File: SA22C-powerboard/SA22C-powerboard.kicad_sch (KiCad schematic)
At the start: 22 parts, among them J1 Barrel_Jack_MountingPin, J4 Conn_01x09_Pin, J5 Conn_01x09_Pin, J6 Conn_01x02_Pin, J7 Conn_02x09_Odd_Even_MountingP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, U1 LM7805_TO220

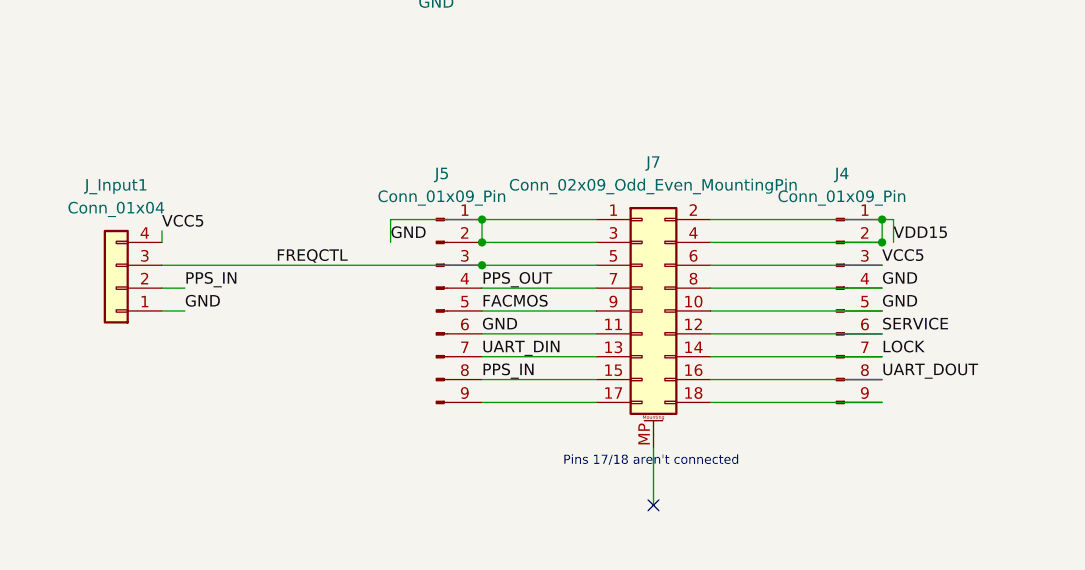
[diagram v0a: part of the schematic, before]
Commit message: Placement drafted, now on to gnd plane and cleanup/simplification
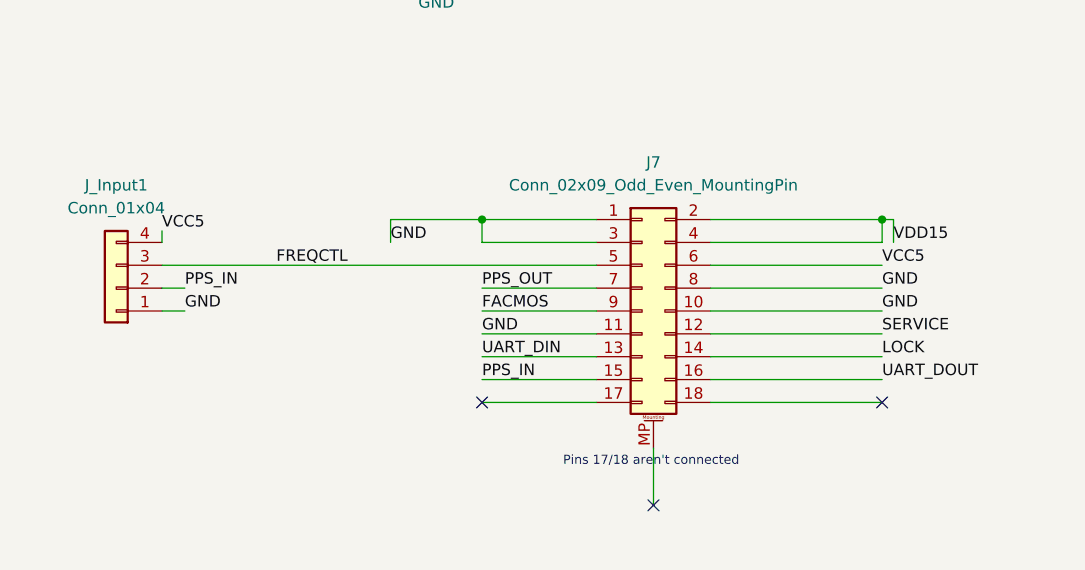
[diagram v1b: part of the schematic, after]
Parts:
- removed J4, J5: Conn_01x09_Pin, Connector_PinHeader_2.54mm:PinHeader_1x09_P2.54mm_Vertical, symbol Connector:Conn_01x09_Pin
- C3: footprint Capacitor_THT:C_Radial_D5.0mm_H11.0mm_P2.00mm -> Capacitor_SMD:CP_Elec_10x10
- C5: footprint Capacitor_SMD:CP_Elec_10x10 -> Capacitor_THT:C_Radial_D5.0mm_H11.0mm_P2.00mm
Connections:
- no-connect marks 1 -> 3
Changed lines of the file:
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@@
-	)
-	(junction
-		(at 118.11 85.09)
-		(diameter 0)
-		(color 0 0 0 0)
 	)
 	(junction
@@
 	)
 	(junction
-		(at 118.11 87.63)
-		(diameter 0)
-		(color 0 0 0 0)
-	)
-	(junction
 		(at 82.55 53.34)
 		(diameter 0)
@@
 	)
 	(junction
-		(at 162.56 85.09)
-		(diameter 0)
-		(color 0 0 0 0)
-	)
-	(junction
 		(at 76.2 34.29)
 		(diameter 0)
@@
 	)
 	(no_connect
+		(at 118.11 102.87)
+	)
+	(no_connect
 		(at 137.16 114.3)
 	)
+	(no_connect
+		(at 162.56 102.87)
+	)
 	(wire
 		(pts
@@
 	(wire
 		(pts
-			(xy 118.11 87.63) (xy 130.81 87.63)
+			(xy 82.55 87.63) (xy 130.81 87.63)
 		)
 		(stroke
@@
 		(pts
 			(xy 82.55 83.82) (xy 82.55 85.09)
-		)
-		(stroke
-			(width 0)
-			(type default)
-		)
-	)
-	(wire
-		(pts
-			(xy 82.55 87.63) (xy 118.11 87.63)
 		)
 		(stroke
@@
 	)
 	(symbol
-		(lib_id "Connector:Conn_01x09_Pin")
-		(at 113.03 92.71 0)
-		(unit 1)
-		(exclude_from_sim no)
-		(in_bom yes)
-		(on_board yes)
-		(dnp no)
-		(fields_autoplaced yes)
-		(property "Reference" "J5"
-			(at 113.665 77.47 0)
-			(effects
-				(font
-					(size 1.27 1.27)
-				)
-			)
-		)
-		(property "Value" "Conn_01x09_Pin"
-			(at 113.665 80.01 0)
-			(effects
-				(font
-					(size 1.27 1.27)
-				)
-			)
-		)
-		(property "Footprint" "Connector_PinHeader_2.54mm:PinHeader_1x09_P2.54mm_Vertical"
-			(at 113.03 92.71 0)
-			(effects
-				(font
-					(size 1.27 1.27)
-				)
-				(hide yes)
-			)
-		)
-		(property "Datasheet" "~"
-			(at 113.03 92.71 0)
-			(effects
-				(font
-					(size 1.27 1.27)
-				)
-				(hide yes)
-			)
-		)
-		(property "Description" "Generic connector, single row, 01x09, script generated"
-			(at 113.03 92.71 0)
-			(effects
-				(font
-					(size 1.27 1.27)
-				)
-				(hide yes)
-			)
-		)
-		(pin "1"
-		)
-		(pin "4"
-		)
-		(pin "2"
-		)
-		(pin "3"
-		)
-		(pin "5"
-		)
-		(pin "6"
-		)
-		(pin "7"
-		)
-		(pin "9"
-		)
-		(pin "8"
-		)
-		(instances
-			(project "SA22C-powerboard"
-				(path "/399af68e-5a20-469a-aa94-44ecde45092b"
-					(reference "J5")
-					(unit 1)
-				)
-			)
-		)
-	)
-	(symbol
 		(lib_id "Device:R")
 		(at 199.39 57.15 0)
@@
 			)
 		)
-		(property "Footprint" "Capacitor_THT:C_Radial_D5.0mm_H11.0mm_P2.00mm"
+		(property "Footprint" "Capacitor_SMD:CP_Elec_10x10"
 			(at 92.4052 45.72 0)
 			(effects
@@
 	)
 	(symbol
-		(lib_id "Connector:Conn_01x09_Pin")
-		(at 157.48 92.71 0)
-		(unit 1)
-		(exclude_from_sim no)
-		(in_bom yes)
-		(on_board yes)
-		(dnp no)
-		(fields_autoplaced yes)
-		(property "Reference" "J4"
-			(at 158.115 77.47 0)
-			(effects
-				(font
-					(size 1.27 1.27)
-				)
-			)
-		)
-		(property "Value" "Conn_01x09_Pin"
-			(at 158.115 80.01 0)
-			(effects
-				(font
-					(size 1.27 1.27)
-				)
-			)
-		)
-		(property "Footprint" "Connector_PinHeader_2.54mm:PinHeader_1x09_P2.54mm_Vertical"
-			(at 157.48 92.71 0)
-			(effects
-				(font
-					(size 1.27 1.27)
-				)
-				(hide yes)
-			)
-		)
-		(property "Datasheet" "~"
-			(at 157.48 92.71 0)
-			(effects
-				(font
-					(size 1.27 1.27)
-				)
-				(hide yes)
-			)
-		)
-		(property "Description" "Generic connector, single row, 01x09, script generated"
-			(at 157.48 92.71 0)
-			(effects
-				(font
-					(size 1.27 1.27)
-				)
-				(hide yes)
-			)
-		)
-		(pin "1"
-		)
-		(pin "4"
-		)
-		(pin "2"
-		)
-		(pin "3"
-		)
-		(pin "5"
-		)
-		(pin "6"
-		)
-		(pin "7"
-		)
-		(pin "9"
-		)
-		(pin "8"
-		)
-		(instances
-			(project "SA22C-powerboard"
-				(path "/399af68e-5a20-469a-aa94-44ecde45092b"
-					(reference "J4")
-					(unit 1)
-				)
-			)
-		)
-	)
-	(symbol
 		(lib_id "Device:C_Polarized")
 		(at 151.13 41.91 0)
@@
 			)
 		)
-		(property "Footprint" "Capacitor_SMD:CP_Elec_10x10"
+		(property "Footprint" "Capacitor_THT:C_Radial_D5.0mm_H11.0mm_P2.00mm"
 			(at 152.0952 45.72 0)
 			(effects
